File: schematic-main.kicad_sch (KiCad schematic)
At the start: 14 parts, among them J1 Conn_01x02, J2 Conn_01x03, J3 Conn_01x02, J6 Conn_01x04, P1 USB_C_Plug_USB2.0

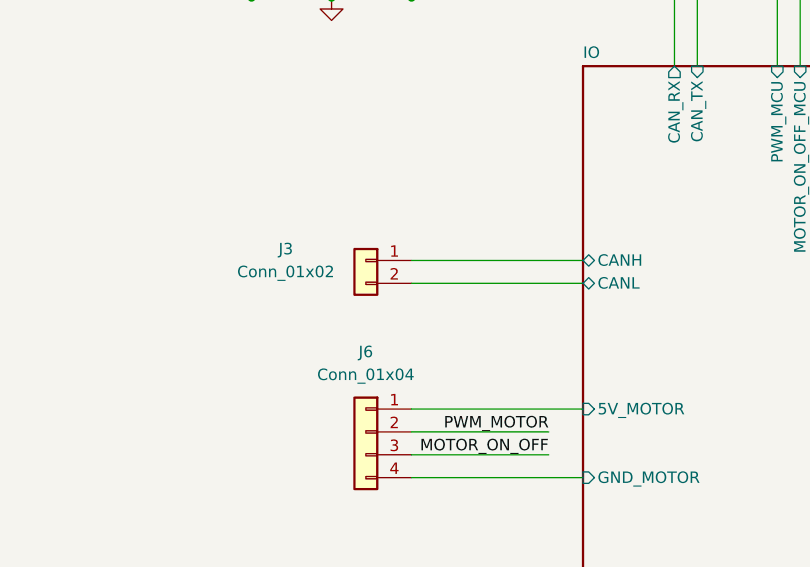
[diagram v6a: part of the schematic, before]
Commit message: Changing placements of SolderJumper, CAN connector to 3 pins, traces 0,4
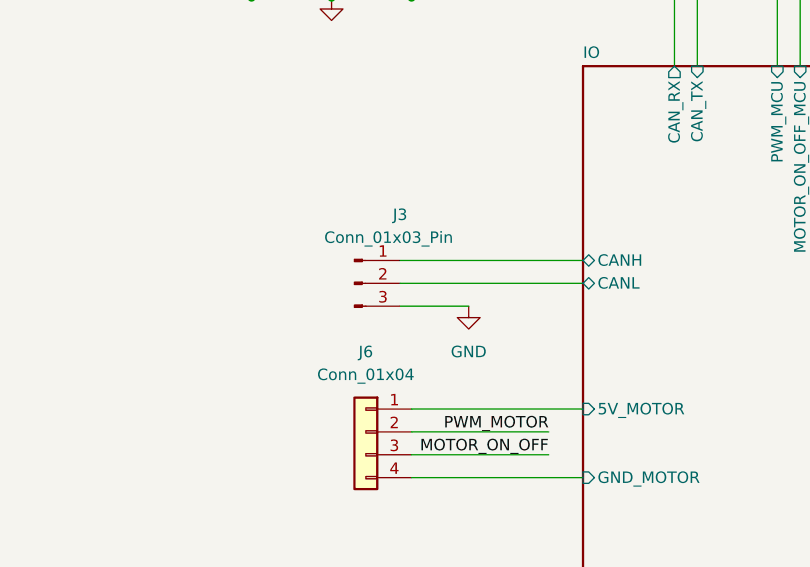
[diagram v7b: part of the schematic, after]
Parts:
- removed J3: Conn_01x02, Connector_Molex:39-30-102Y, symbol Connector_Generic:Conn_01x02
- added J3: Conn_01x03_Pin, Connector_Molex:39303035, symbol Connector:Conn_01x03_Pin
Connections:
- net GND: now also J3.3 (Pin_3)
- net IO/CANH: now also J3.1 (Pin_1)
- net IO/CANL: now also J3.2 (Pin_2)
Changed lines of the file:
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@@
     (stroke (width 0) (type default))
   )
-  (wire (pts (xy 115.57 125.73) (xy 134.62 125.73))
+  (wire (pts (xy 114.3 125.73) (xy 134.62 125.73))
     (stroke (width 0) (type default))
   )
@@
     (stroke (width 0) (type default))
   )
+  (wire (pts (xy 121.92 130.81) (xy 114.3 130.81))
+    (stroke (width 0) (type default))
+  )
   (wire (pts (xy 46.99 35.56) (xy 49.53 35.56))
     (stroke (width 0) (type default))
@@
     (stroke (width 0) (type default))
   )
-  (wire (pts (xy 115.57 128.27) (xy 134.62 128.27))
+  (wire (pts (xy 114.3 128.27) (xy 134.62 128.27))
     (stroke (width 0) (type default))
   )
@@
     )
   )
-  (symbol (lib_id "Connector_Generic:Conn_01x02") (at 110.49 125.73 0) (mirror y) (unit 1)
-    (in_bom yes) (on_board yes) (dnp no)
-    (property "Reference" "J3" (at 101.6 124.46 0)
-      (effects (font (size 1.27 1.27)))
-    )
-    (property "Value" "Conn_01x02" (at 101.6 127 0)
-      (effects (font (size 1.27 1.27)))
-    )
-    (property "Footprint" "Connector_Molex:39-30-102Y" (at 110.49 125.73 0)
-      (effects (font (size 1.27 1.27)) hide)
-    )
-    (property "Datasheet" "~" (at 110.49 125.73 0)
-      (effects (font (size 1.27 1.27)) hide)
-    )
-    (pin "1")
-    (pin "2")
-    (instances
-      (project "schematic-main"
-        (path "/c9ad7189-d3b2-414a-9743-efd8e57cd755"
-          (reference "J3") (unit 1)
-        )
-      )
-    )
-  )
   (symbol (lib_id "Connector_Generic:Conn_01x02") (at 41.91 33.02 0) (mirror y) (unit 1)
     (in_bom yes) (on_board yes) (dnp no)
@@
     )
   )
+  (symbol (lib_id "power:GND") (at 121.92 130.81 0) (unit 1)
+    (in_bom yes) (on_board yes) (dnp no) (fields_autoplaced)
+    (property "Reference" "#PWR06" (at 121.92 137.16 0)
+      (effects (font (size 1.27 1.27)) hide)
+    )
+    (property "Value" "GND" (at 121.92 135.89 0)
+      (effects (font (size 1.27 1.27)))
+    )
+    (property "Footprint" "" (at 121.92 130.81 0)
+      (effects (font (size 1.27 1.27)) hide)
+    )
+    (property "Datasheet" "" (at 121.92 130.81 0)
+      (effects (font (size 1.27 1.27)) hide)
+    )
+    (pin "1")
+    (instances
+      (project "schematic-main"
+        (path "/c9ad7189-d3b2-414a-9743-efd8e57cd755"
+          (reference "#PWR06") (unit 1)
+        )
+      )
+    )
+  )
   (symbol (lib_id "power:PWR_FLAG") (at 48.26 40.64 90) (unit 1)
     (in_bom yes) (on_board yes) (dnp no) (fields_autoplaced)
@@
         )
       )
+    )
+  )
+  (symbol (lib_id "Connector:Conn_01x03_Pin") (at 109.22 128.27 0) (unit 1)
+    (in_bom yes) (on_board yes) (dnp no)
+    (property "Reference" "J3" (at 114.3 120.65 0)
+      (effects (font (size 1.27 1.27)))
+    )
+    (property "Value" "Conn_01x03_Pin" (at 113.03 123.19 0)
+      (effects (font (size 1.27 1.27)))
+    )
+    (property "Footprint" "Connector_Molex:39303035" (at 109.22 128.27 0)
+      (effects (font (size 1.27 1.27)) hide)
+    )
+    (property "Datasheet" "~" (at 109.22 128.27 0)
+      (effects (font (size 1.27 1.27)) hide)
+    )
+    (pin "1")
+    (pin "2")
+    (pin "3")
+    (instances
+      (project "schematic-main"
+        (path "/c9ad7189-d3b2-414a-9743-efd8e57cd755"
+          (reference "J3") (unit 1)
+        )
+      )

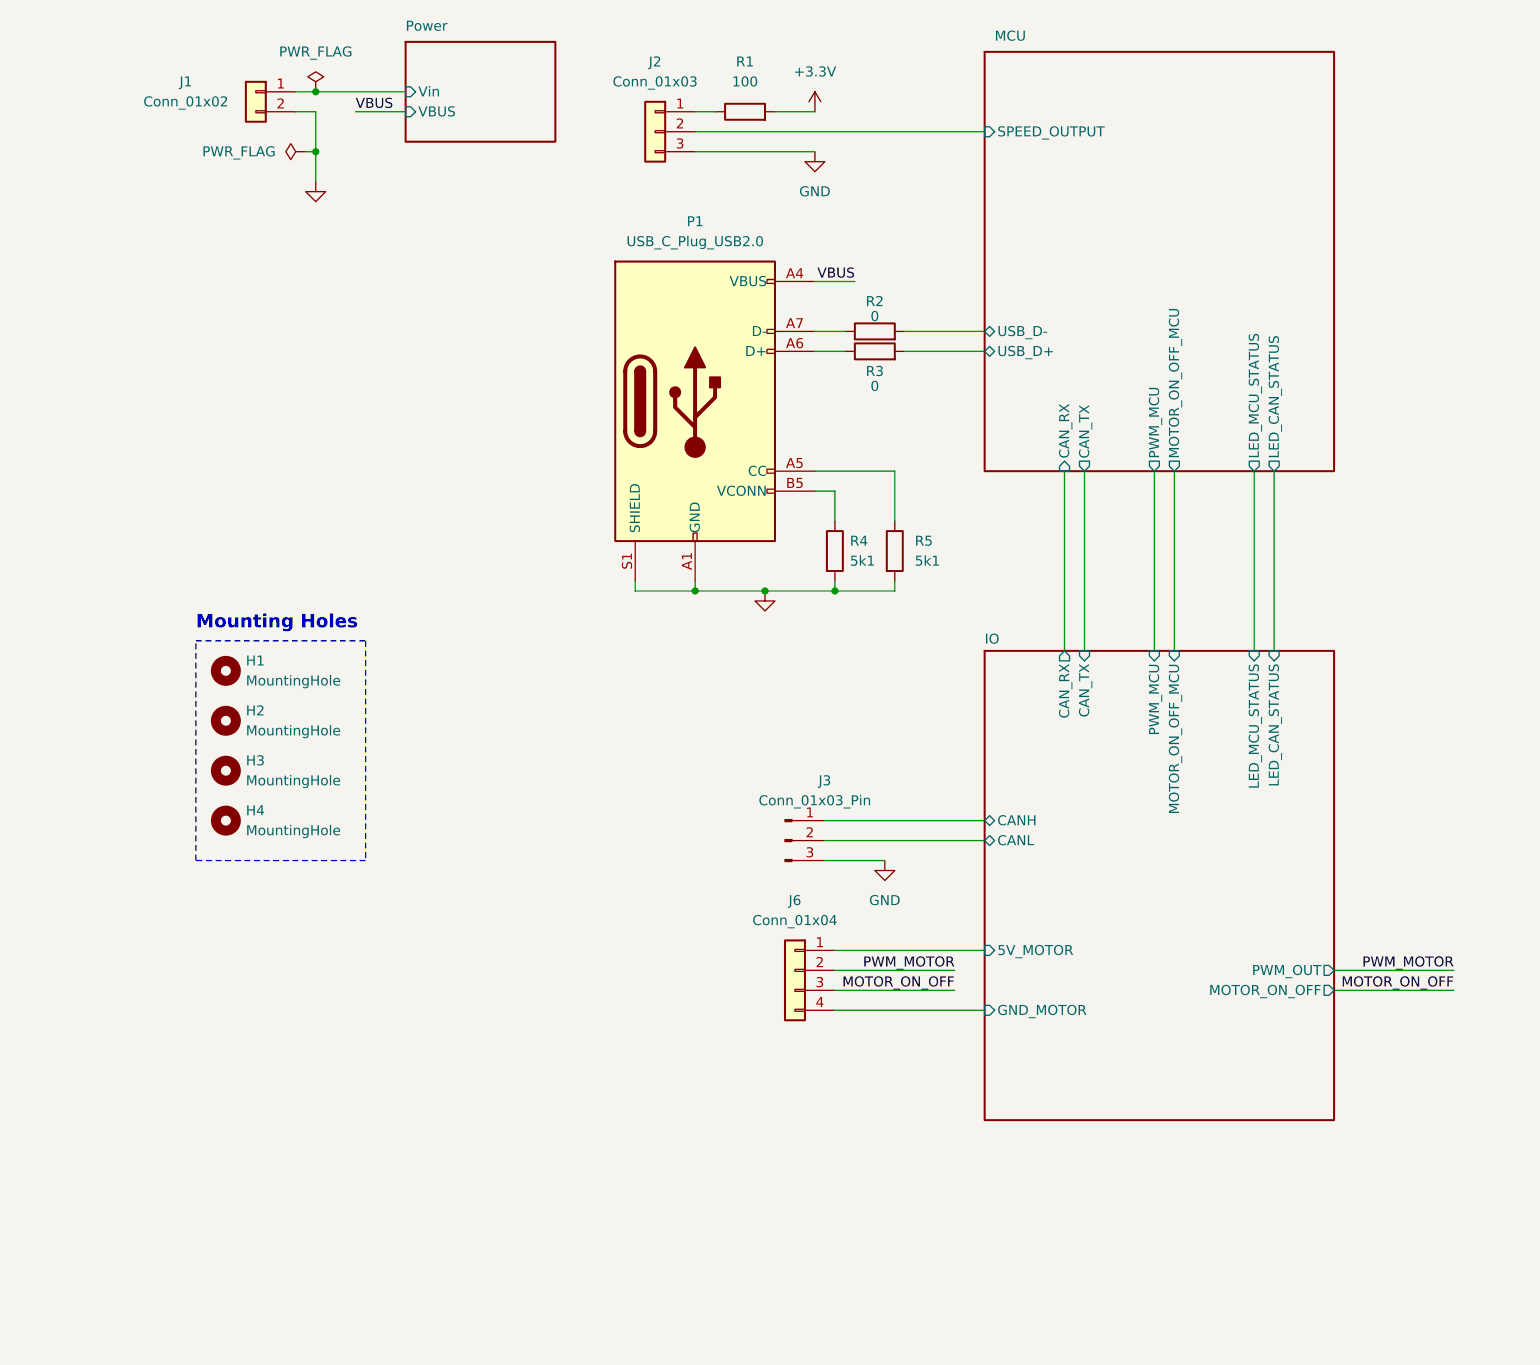
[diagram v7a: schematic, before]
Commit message: Add test pins for: 3,3V, 5V, 12V and GND
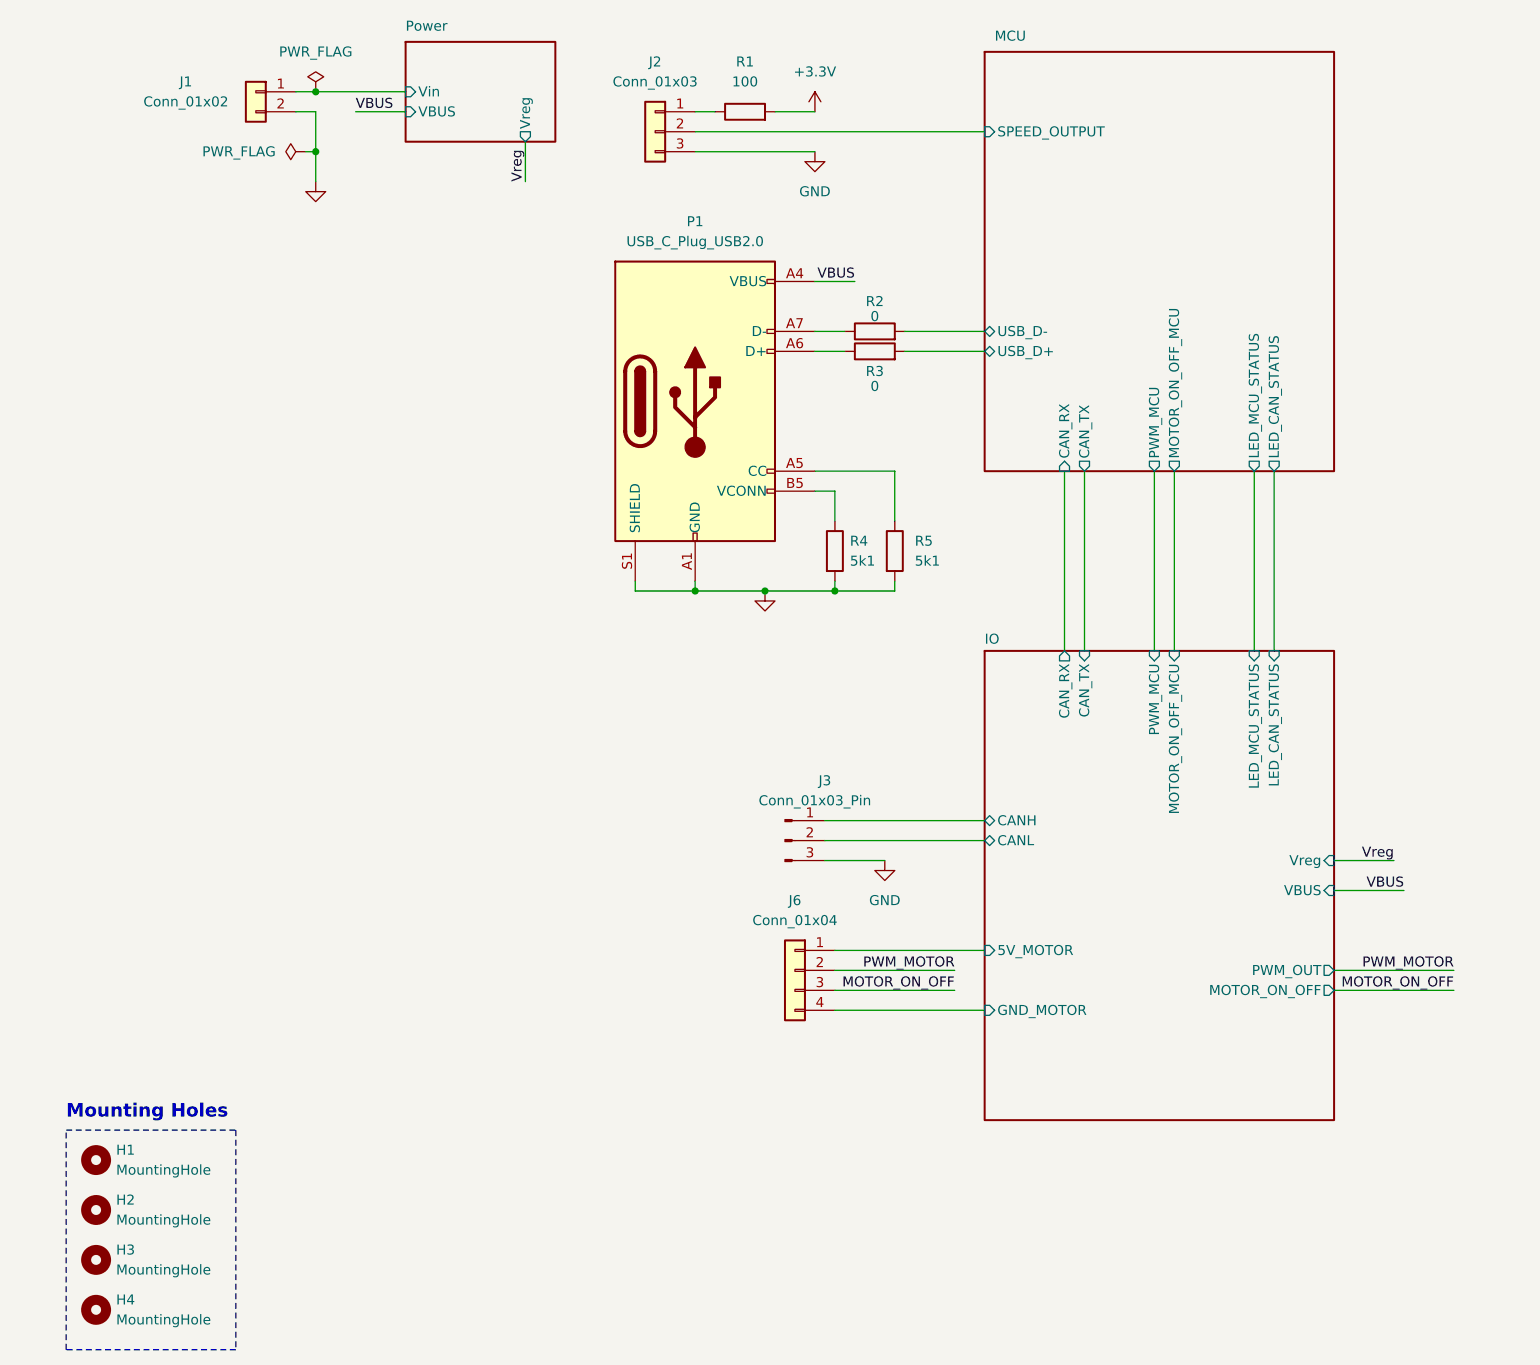
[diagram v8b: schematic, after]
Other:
- sheet IO ports: added VBUS, Vreg; removed none
- sheet Power  ports: added Vreg; removed none
- moved on the sheet: H1, H2, H3, H4
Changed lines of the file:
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@@
+    (stroke (width 0) (type default))
+  )
+  (wire (pts (xy 76.2 39.37) (xy 76.2 44.45))
+    (stroke (width 0) (type default))
+  )
+  (wire (pts (xy 179.07 134.62) (xy 187.96 134.62))
     (stroke (width 0) (type default))
   )
@@
     (stroke (width 0) (type default))
   )
+  (wire (pts (xy 179.07 130.81) (xy 186.69 130.81))
+    (stroke (width 0) (type default))
+  )
   (wire (pts (xy 115.57 96.52) (xy 123.19 96.52))
     (stroke (width 0) (type default))
@@
     (stroke (width 0) (type default))
   )
-  (rectangle (start 34.29 102.87) (end 55.88 130.81)
+  (rectangle (start 17.78 165.1) (end 39.37 193.04)
     (stroke (width 0) (type dash))
     (fill (type none))
   )
-  (text "Mounting Holes" (at 34.29 101.6 0)
+  (text "Mounting Holes" (at 17.78 163.83 0)
     (effects (font (size 1.7 1.7) (thickness 0.4) bold) (justify left bottom))
   )
@@
     (effects (font (size 1.27 1.27)) (justify right bottom))
   )
+  (label "Vreg" (at 76.2 44.45 90) (fields_autoplaced)
+    (effects (font (size 1.27 1.27)) (justify left bottom))
+  )
   (label "PWM_MOTOR" (at 194.31 144.78 180) (fields_autoplaced)
     (effects (font (size 1.27 1.27)) (justify right bottom))
   )
+  (label "VBUS" (at 187.96 134.62 180) (fields_autoplaced)
+    (effects (font (size 1.27 1.27)) (justify right bottom))
+  )
   (label "MOTOR_ON_OFF" (at 194.31 147.32 180) (fields_autoplaced)
     (effects (font (size 1.27 1.27)) (justify right bottom))
@@
   )
   (label "VBUS" (at 118.11 57.15 180) (fields_autoplaced)
+    (effects (font (size 1.27 1.27)) (justify right bottom))
+  )
+  (label "Vreg" (at 186.69 130.81 180) (fields_autoplaced)
     (effects (font (size 1.27 1.27)) (justify right bottom))
   )
@@
     )
   )
-  (symbol (lib_id "Mechanical:MountingHole") (at 38.1 113.03 0) (unit 1)
-    (in_bom yes) (on_board yes) (dnp no) (fields_autoplaced)
-    (property "Reference" "H2" (at 40.64 111.76 0)
-      (effects (font (size 1.27 1.27)) (justify left))
-    )
-    (property "Value" "MountingHole" (at 40.64 114.3 0)
-      (effects (font (size 1.27 1.27)) (justify left))
-    )
-    (property "Footprint" "MountingHole:MountingHole_2.2mm_M2" (at 38.1 113.03 0)
-      (effects (font (size 1.27 1.27)) hide)
-    )
-    (property "Datasheet" "~" (at 38.1 113.03 0)
+  (symbol (lib_id "Mechanical:MountingHole") (at 21.59 175.26 0) (unit 1)
+    (in_bom yes) (on_board yes) (dnp no) (fields_autoplaced)
+    (property "Reference" "H2" (at 24.13 173.99 0)
+      (effects (font (size 1.27 1.27)) (justify left))
+    )
+    (property "Value" "MountingHole" (at 24.13 176.53 0)
+      (effects (font (size 1.27 1.27)) (justify left))
+    )
+    (property "Footprint" "MountingHole:MountingHole_2.2mm_M2" (at 21.59 175.26 0)
+      (effects (font (size 1.27 1.27)) hide)
+    )
+    (property "Datasheet" "~" (at 21.59 175.26 0)
       (effects (font (size 1.27 1.27)) hide)
     )
@@
     )
   )
-  (symbol (lib_id "Mechanical:MountingHole") (at 38.1 106.68 0) (unit 1)
-    (in_bom yes) (on_board yes) (dnp no) (fields_autoplaced)
-    (property "Reference" "H1" (at 40.64 105.41 0)
-      (effects (font (size 1.27 1.27)) (justify left))
-    )
-    (property "Value" "MountingHole" (at 40.64 107.95 0)
-      (effects (font (size 1.27 1.27)) (justify left))
-    )
-    (property "Footprint" "MountingHole:MountingHole_2.2mm_M2" (at 38.1 106.68 0)
-      (effects (font (size 1.27 1.27)) hide)
-    )
-    (property "Datasheet" "~" (at 38.1 106.68 0)
+  (symbol (lib_id "Mechanical:MountingHole") (at 21.59 168.91 0) (unit 1)
+    (in_bom yes) (on_board yes) (dnp no) (fields_autoplaced)
+    (property "Reference" "H1" (at 24.13 167.64 0)
+      (effects (font (size 1.27 1.27)) (justify left))
+    )
+    (property "Value" "MountingHole" (at 24.13 170.18 0)
+      (effects (font (size 1.27 1.27)) (justify left))
+    )
+    (property "Footprint" "MountingHole:MountingHole_2.2mm_M2" (at 21.59 168.91 0)
+      (effects (font (size 1.27 1.27)) hide)
+    )
+    (property "Datasheet" "~" (at 21.59 168.91 0)
       (effects (font (size 1.27 1.27)) hide)
     )
@@
     )
   )
-  (symbol (lib_id "Mechanical:MountingHole") (at 38.1 125.73 0) (unit 1)
-    (in_bom yes) (on_board yes) (dnp no) (fields_autoplaced)
-    (property "Reference" "H4" (at 40.64 124.46 0)
-      (effects (font (size 1.27 1.27)) (justify left))
-    )
-    (property "Value" "MountingHole" (at 40.64 127 0)
-      (effects (font (size 1.27 1.27)) (justify left))
-    )
-    (property "Footprint" "MountingHole:MountingHole_2.2mm_M2" (at 38.1 125.73 0)
-      (effects (font (size 1.27 1.27)) hide)
-    )
-    (property "Datasheet" "~" (at 38.1 125.73 0)
+  (symbol (lib_id "Mechanical:MountingHole") (at 21.59 187.96 0) (unit 1)
+    (in_bom yes) (on_board yes) (dnp no) (fields_autoplaced)
+    (property "Reference" "H4" (at 24.13 186.69 0)
+      (effects (font (size 1.27 1.27)) (justify left))
+    )
+    (property "Value" "MountingHole" (at 24.13 189.23 0)
+      (effects (font (size 1.27 1.27)) (justify left))
+    )
+    (property "Footprint" "MountingHole:MountingHole_2.2mm_M2" (at 21.59 187.96 0)
+      (effects (font (size 1.27 1.27)) hide)
+    )
+    (property "Datasheet" "~" (at 21.59 187.96 0)
       (effects (font (size 1.27 1.27)) hide)
     )
@@
     )
   )
-  (symbol (lib_id "Mechanical:MountingHole") (at 38.1 119.38 0) (unit 1)
-    (in_bom yes) (on_board yes) (dnp no) (fields_autoplaced)
-    (property "Reference" "H3" (at 40.64 118.11 0)
-      (effects (font (size 1.27 1.27)) (justify left))
-    )
-    (property "Value" "MountingHole" (at 40.64 120.65 0)
-      (effects (font (size 1.27 1.27)) (justify left))
-    )
-    (property "Footprint" "MountingHole:MountingHole_2.2mm_M2" (at 38.1 119.38 0)
-      (effects (font (size 1.27 1.27)) hide)
-    )
-    (property "Datasheet" "~" (at 38.1 119.38 0)
+  (symbol (lib_id "Mechanical:MountingHole") (at 21.59 181.61 0) (unit 1)
+    (in_bom yes) (on_board yes) (dnp no) (fields_autoplaced)
+    (property "Reference" "H3" (at 24.13 180.34 0)
+      (effects (font (size 1.27 1.27)) (justify left))
+    )
+    (property "Value" "MountingHole" (at 24.13 182.88 0)
+      (effects (font (size 1.27 1.27)) (justify left))
+    )
+    (property "Footprint" "MountingHole:MountingHole_2.2mm_M2" (at 21.59 181.61 0)
+      (effects (font (size 1.27 1.27)) hide)
+    )
+    (property "Datasheet" "~" (at 21.59 181.61 0)
       (effects (font (size 1.27 1.27)) hide)
     )
@@
       (effects (font (size 1.27 1.27)) (justify right))
     )
+    (pin "VBUS" input (at 179.07 134.62 0)
+      (effects (font (size 1.27 1.27)) (justify right))
+    )
+    (pin "Vreg" input (at 179.07 130.81 0)
+      (effects (font (size 1.27 1.27)) (justify right))
+    )
     (instances
       (project "schematic-main"
@@
       (effects (font (size 1.27 1.27)) (justify left))
     )
+    (pin "Vreg" output (at 76.2 39.37 270)
+      (effects (font (size 1.27 1.27)) (justify left))
+    )
